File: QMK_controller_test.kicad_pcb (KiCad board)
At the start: 2 copper layers, 12.1 x 22.8 mm, 14 parts, among them J1 USB_A, J3 BOOT0_HI_JMP, U1 STM32F042G6Ux, U2 XC6206PxxxMR

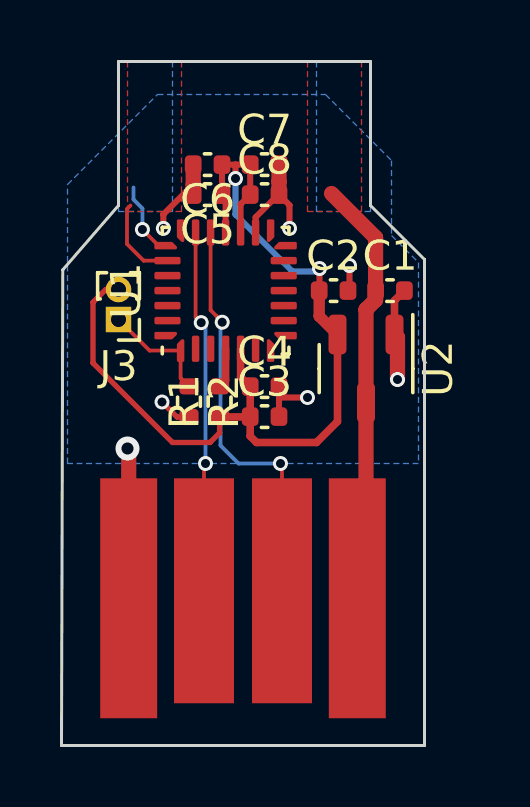
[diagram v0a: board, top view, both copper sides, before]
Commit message: V0.2 - Fixed broken DIN 5 pinout. Fixed SWD conflict pinout (PB3 - DATA, PA15 - CLOCK). Also added SWD testpoints.
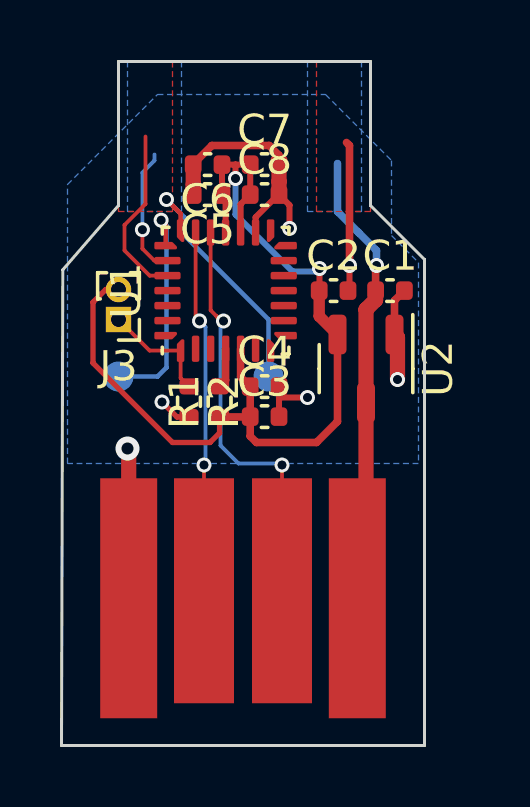
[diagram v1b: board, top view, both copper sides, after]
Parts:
- added TP1: SWDIO, TestPoint:TestPoint_Pad_D1.0mm, B.Cu at (142.5, 92.5)
- added TP2: SWCLK, TestPoint:TestPoint_Pad_D1.0mm, B.Cu at (137.5, 92.5)
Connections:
- U1 pad 21: unconnected-(U1-PA13-Pad21) -> /SWDIO
- U1 pad 22: /TERM_DATA -> /SWCLK
- U1 pad 24: unconnected-(U1-PB3-Pad24) -> /TERM_DATA
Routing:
- net /SWDIO: track 0.00 -> 8.54 mm, vias 0 -> 1
- net /SWCLK: track 0.00 -> 7.62 mm, vias 0 -> 1
- net GND: track 18.8 -> 25.3 mm, vias 7 -> 6
- net /TERM_DATA: track 2.52 -> 5.87 mm, vias 1 -> 0
- net /TERM_CLOCK: track 2.91 -> 4.31 mm, vias 0 -> 1
- net +5V: track 14.4 -> 15.3 mm, vias 0 -> 1
- added copper zone on B.Cu, net +5V
- added copper zone on B.Cu, net /TERM_CLOCK
- added copper zone on F.Cu, net /TERM_DATA
- added copper zone on F.Cu, net GND
- removed copper zone on F.Cu, net +5V
- removed copper zone on F.Cu, net /TERM_CLOCK
- removed copper zone on B.Cu, net /TERM_DATA
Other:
- board text added: "BOOT"
